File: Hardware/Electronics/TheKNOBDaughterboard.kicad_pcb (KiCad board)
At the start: 2 copper layers, 58 x 28 mm, 52 parts, among them J1 Conn_01x02_Female, J2 USB_C_Receptacle_USB2.0, J3 Conn_01x03, J4 Conn_01x04, J5 Conn_01x11, Q1 Q_NMOS_GSD, Q2 Q_NMOS_GSD, SW1 SW_Push, SW2 SW_Push, U1 MCP73831-5-OT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

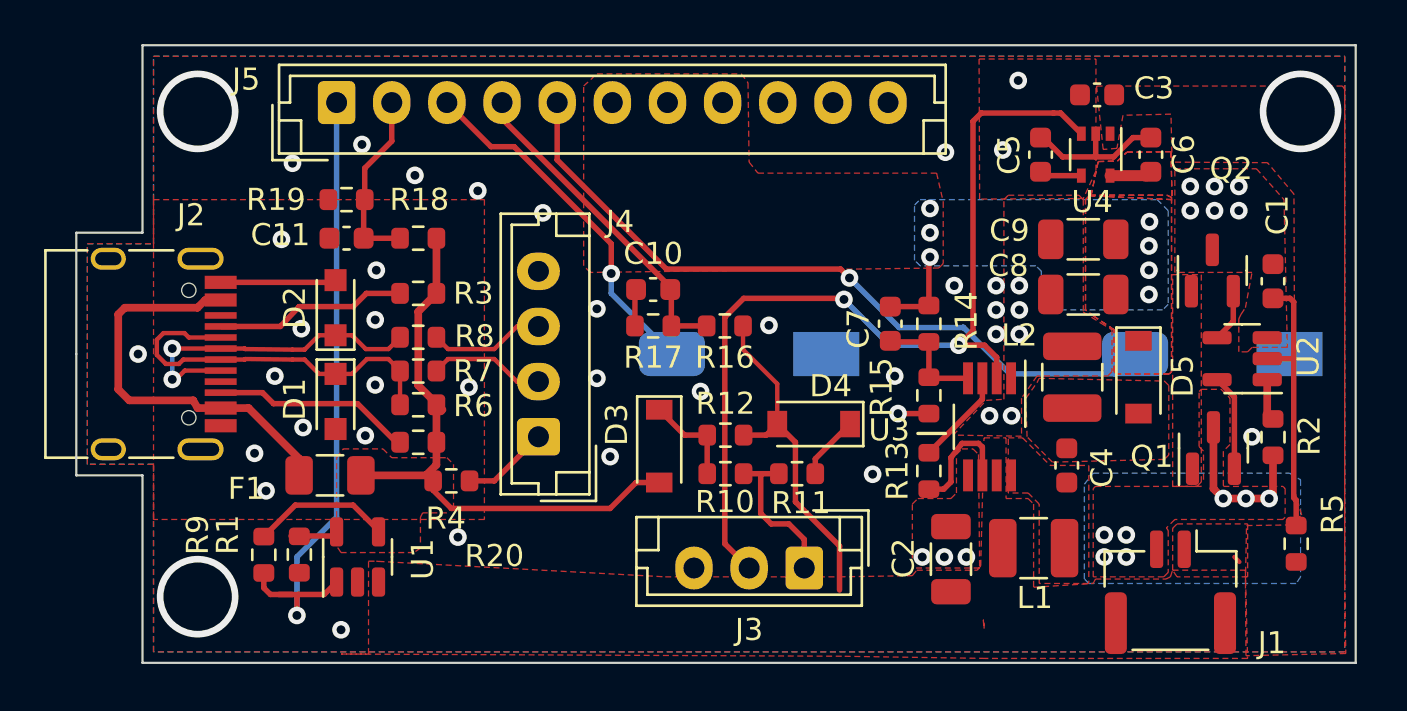
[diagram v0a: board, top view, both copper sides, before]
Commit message: add 3d files, changes to sch and pcb
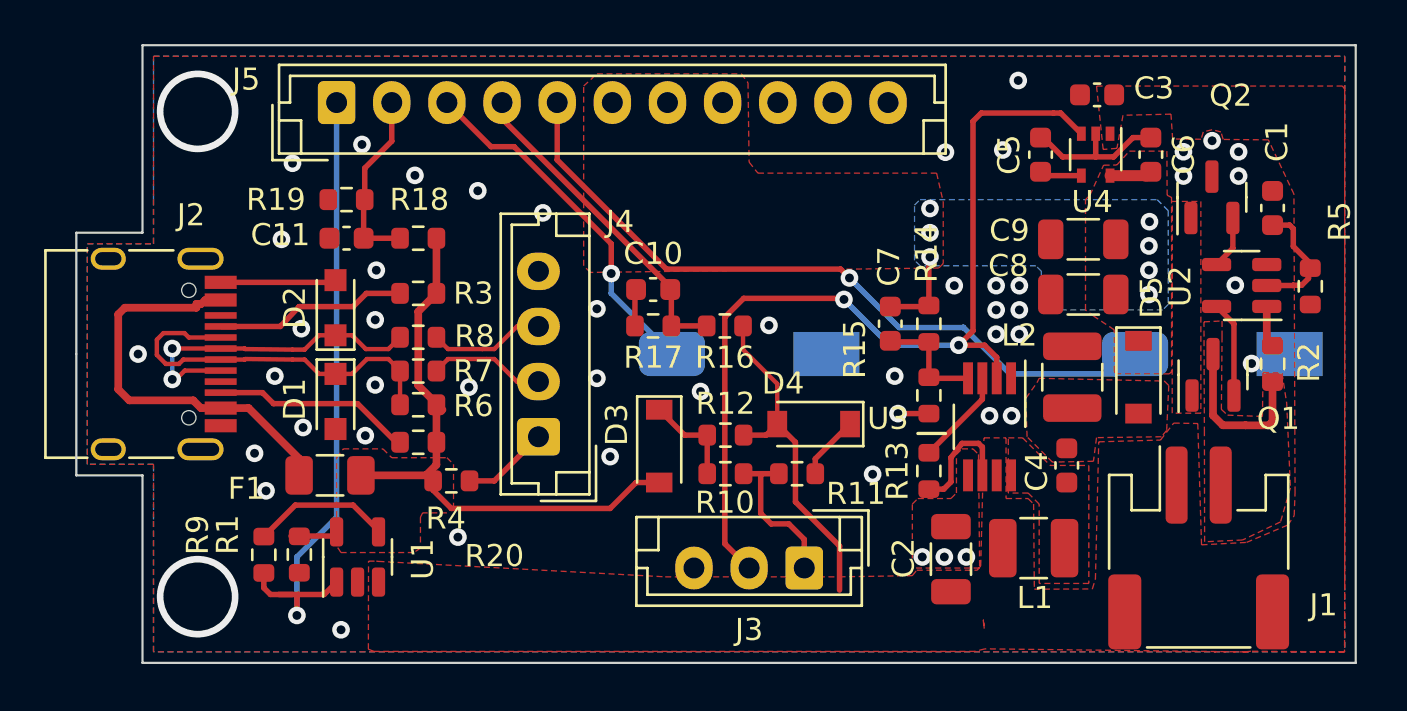
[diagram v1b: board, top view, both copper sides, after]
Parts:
- J1: footprint Connector_JST:JST_GH_BM02B-GHS-TBT_1x02-1MP_P1.25mm_Vertical -> Connector_JST:JST_PH_S2B-PH-SM4-TB_1x02-1MP_P2.00mm_Horizontal
- moved R5 11.7 mm to (125.4, 96.9)
- moved C1 3.32 mm to (123.7, 93.4)
- moved Q1 3.32 mm to (121.0, 100.9)
- moved Q2 3.32 mm to (121.0, 92.9)
- moved R2 3.32 mm to (123.7, 100.4)
- moved U2 3.32 mm to (122.3, 96.9)
- moved J1 2.38 mm to (120.4, 108.8), turned to 0 degrees
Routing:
- net Net-(C1-Pad1): track 12.4 -> 5.57 mm
- net /VBat-: vias 7 -> 0
- net GND: vias 52 -> 51
- removed copper zone on B.Cu, net /VBat-

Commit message: Batt Protection and SMPS chip changed due to chip shortage
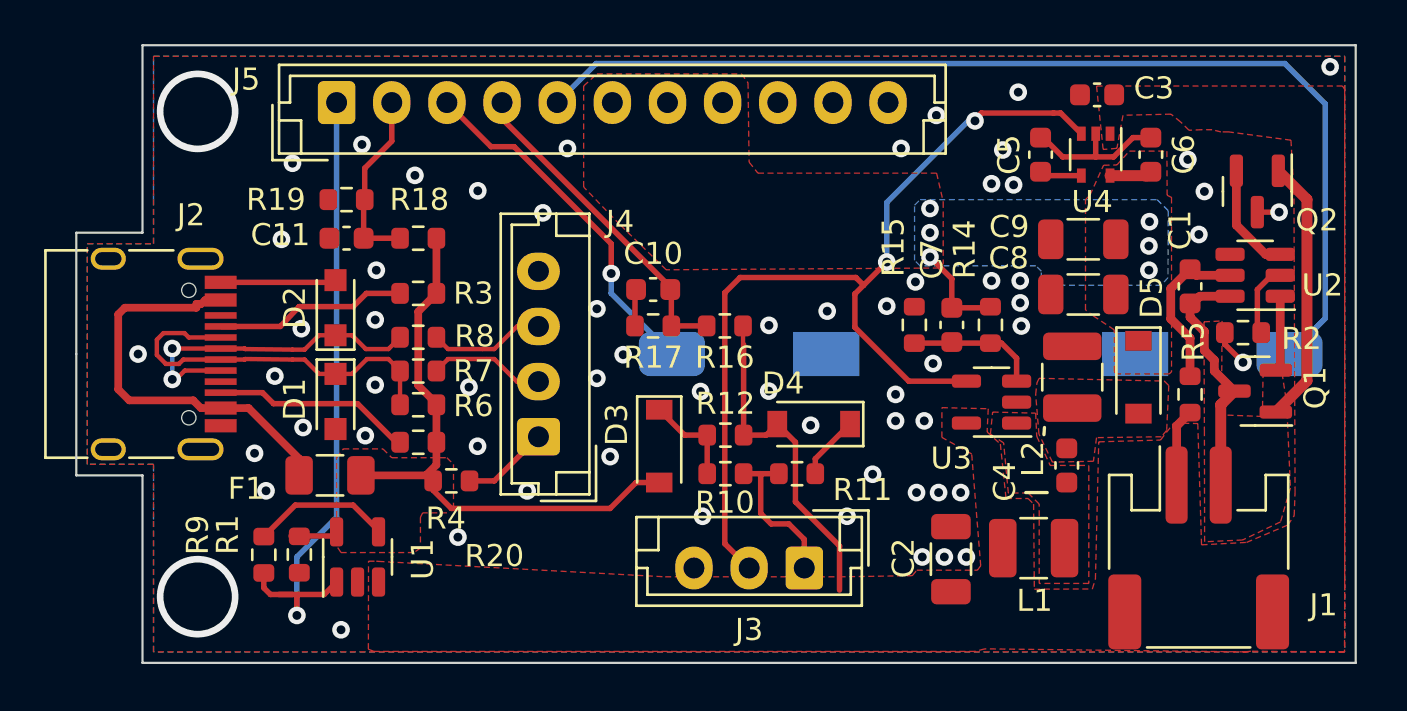
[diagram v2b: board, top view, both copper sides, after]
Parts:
- removed R13: 80k, Resistor_SMD:R_0603_1608Metric
- C2, C8, C9: value 33uF -> 47uF
- R14: value 150k -> 16k
- R15: value 91k -> 10k
- R16, R18: value 460k -> 470k
- R2: value 2.7k -> 1k
- R9: value 5k -> 10k
- U2: value AP9101CK -> DW01; footprint Package_TO_SOT_SMD:SOT-23-5 -> Package_TO_SOT_SMD:SOT-23-6
- U3: value LM2621 -> LMR62421XMF; footprint Package_SO:VSSOP-8_3.0x3.0mm_P0.65mm -> Package_TO_SOT_SMD:SOT-23-5
- moved R5 7.33 mm to (120.0, 101.8)
- moved C1 5.16 mm to (120.0, 96.9), turned to -90 degrees
- moved R15 3.26 mm to (107.5, 98.7)
- moved C7 2.79 mm to (109.2, 98.7)
- moved R14 2.79 mm to (110.9, 98.7)
- moved Q2 2.08 mm to (123.0, 92.6), turned to -90 degrees
- moved Q1 2.05 mm to (122.9, 101.7), turned to 180 degrees
- moved R2 1.95 mm to (122.4, 99.0), turned to 180 degrees
- moved U3 1.12 mm to (111.0, 102.2), turned to 180 degrees
- moved U2 0.77 mm to (122.9, 96.4)
- turned SW2 to 180 degrees
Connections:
- C1 pad 2: GND -> /VBat-
- C7 pad 2: Net-(C7-Pad2) -> /U3_FB
- Q1 pad 2: Net-(Q1-Pad2) -> /U2_OD
- Q2 pad 2: Net-(Q2-Pad2) -> /U2_OC
- R14 pad 2: Net-(C7-Pad2) -> /U3_FB
- R15 pad 1: Net-(C7-Pad2) -> GND
- R15 pad 2: GND -> /U3_FB
- R2 pad 1: Net-(R2-Pad1) -> /U2_CS
- R2 pad 2: /VBat- -> GND
- U2 pad 1: Net-(R2-Pad1) -> /U2_OD
- U2 pad 2: Net-(C1-Pad1) -> /U2_CS
- U2 pad 3: GND -> /U2_OC
- U2 pad 4: Net-(Q2-Pad2) -> unconnected-(U2-Pad4)
- U2 pad 5: Net-(Q1-Pad2) -> Net-(C1-Pad1)
- U3 pad 1: GND -> /U3_SW
- U3 pad 2: /SwitchEn -> GND
- U3 pad 3: Net-(R13-Pad2) -> /U3_FB
- U3 pad 4: Net-(C7-Pad2) -> /SwitchEn
- U3 pad 5: GND -> /VBat+
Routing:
- net /FunctionButton: track 33.2 -> 48.3 mm, vias 1 -> 0
- net Net-(Q1-Pad1): track 0.00 -> 12.1 mm
- net /U3_FB: track 0.00 -> 6.00 mm
- net Net-(R13-Pad1): track 5.33 -> 0.00 mm
- net Net-(C7-Pad2): track 5.17 -> 0.00 mm
- net /U2_OC: track 0.00 -> 5.00 mm
- net Net-(R13-Pad2): track 4.38 -> 0.00 mm
- net Net-(Q1-Pad2): track 4.36 -> 0.00 mm
- net /VBat-: track 7.71 -> 11.3 mm
- net /VBat+: track 15.5 -> 19.0 mm
- net /U2_OD: track 0.00 -> 3.43 mm
- net /U2_CS: track 0.00 -> 3.33 mm
- net Net-(Q2-Pad2): track 2.42 -> 0.00 mm
- net Net-(C1-Pad1): track 5.57 -> 7.50 mm
- net Net-(R2-Pad1): track 1.89 -> 0.00 mm
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- removed copper zone on F.Cu, net Net-(Q1-Pad1)
